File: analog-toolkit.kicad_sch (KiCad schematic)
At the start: 53 parts, among them J1 USB_C, J2 IO, J3 UART, J4 I2C, J5 VBUS, J6 3.3V, J7 OPAMP, J8 ADC, P1 TC2030, Q1 AO3400A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

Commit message: updated kicad files
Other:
- company: (none) -> Jana Hemsing
- title: (none) -> analog-toolkit

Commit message: updated kicad files
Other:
- note added: "20k"
- note added: "3k9"
- note added: "this is fine"

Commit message: updated version
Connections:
- no-connect marks 2 -> 3
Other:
- moved on the sheet: C1, C2, C3, C4, C5, C6, C7, D1, F1, FB1, J1, P1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

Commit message: bumped improved version
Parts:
- C10, C11, C12, C13, C8, C9: value 100n -> 10n
- U3: value STM32G431xB -> STM32G431KBT6
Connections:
- net LED1: now also D1.2 (GK), D1.4 (BA); no longer D1.1 (RK), D1.5 (GA)
- net at Q1.3 (D): now also D1.6 (RA); no longer D1.3 (BK)
- net at R4.2: now also D1.1 (RK); no longer D1.4 (BA)
- net at R2.2: now also D1.3 (BK); no longer D1.6 (RA)
- net at R3.1: now also D1.5 (GA); no longer D1.2 (GK)
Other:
- moved on the sheet: D1
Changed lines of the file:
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@@
 			)
 		)
-		(property "Value" "100n"
+		(property "Value" "10n"
 			(at 210.82 146.05 90)
 			(effects
@@
 			)
 		)
-		(property "Value" "STM32G431xB"
+		(property "Value" "STM32G431KBT6"
 			(at 121.92 105.41 0)
 			(effects
@@
 			)
 		)
-		(property "Value" "100n"
+		(property "Value" "10n"
 			(at 208.28 146.05 90)
 			(effects
@@
 			)
 		)
-		(property "Value" "100n"
+		(property "Value" "10n"
 			(at 213.36 146.05 90)
 			(effects
@@
 			)
 		)
-		(property "Value" "100n"
+		(property "Value" "10n"
 			(at 203.2 146.05 90)
 			(effects
@@
 			)
 		)
-		(property "Value" "100n"
+		(property "Value" "10n"
 			(at 205.74 146.05 90)
 			(effects
@@
 			)
 		)
-		(property "Value" "100n"
+		(property "Value" "10n"
 			(at 200.66 146.05 90)
 			(effects
@@
 	(symbol
 		(lib_id "Device:LED_RGB")
-		(at 143.51 59.69 90)
+		(at 143.51 59.69 270)
 		(unit 1)
 		(exclude_from_sim no)
@@
 		(fields_autoplaced yes)
 		(property "Reference" "D1"
-			(at 152.4 58.4199 90)
+			(at 153.67 58.4199 90)
 			(effects
 				(font
 					(size 1.27 1.27)
 				)
-				(justify right)
+				(justify left)
 			)
 		)
 		(property "Value" "LED_RGB"
-			(at 152.4 60.9599 90)
+			(at 153.67 60.9599 90)
 			(effects
 				(font
 					(size 1.27 1.27)
 				)
-				(justify right)
+				(justify left)
 			)
 		)
 		(property "Footprint" "LED_SMD:LED_RGB_5050-6"
-			(at 144.78 59.69 0)
+			(at 142.24 59.69 0)
 			(effects
 				(font
@@
 		)
 		(property "Datasheet" "~"
-			(at 144.78 59.69 0)
+			(at 142.24 59.69 0)
 			(effects
 				(font

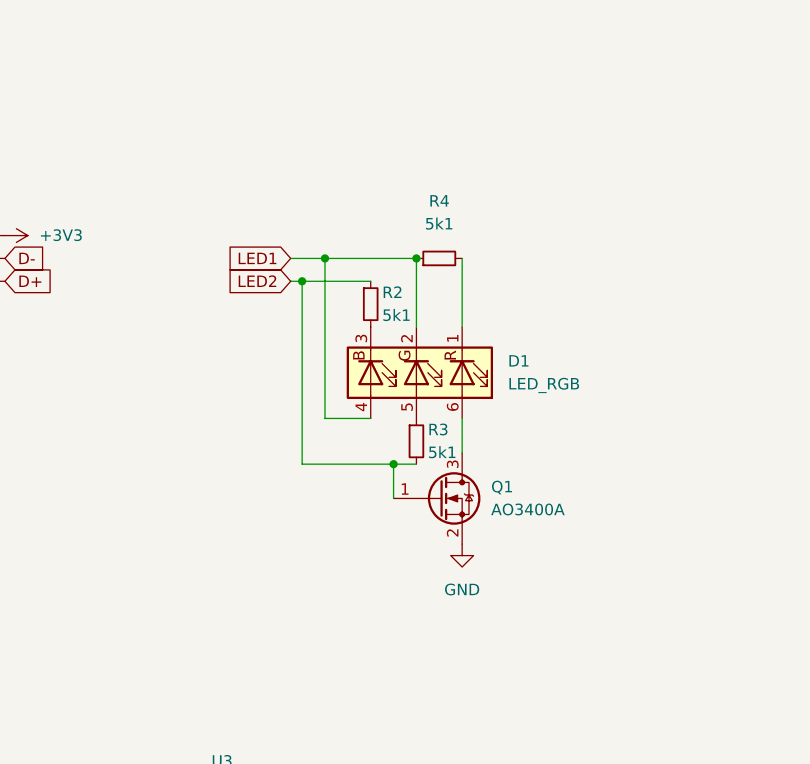
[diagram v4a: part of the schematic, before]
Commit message: updated boards, replaced RGB led
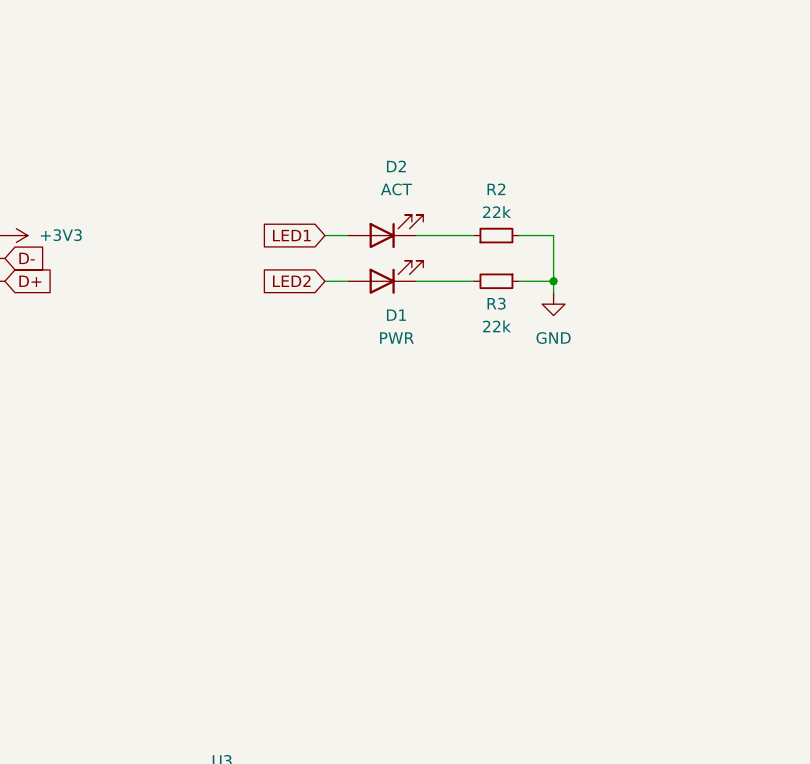
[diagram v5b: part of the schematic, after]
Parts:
- removed D1: LED_RGB, LED_SMD:LED_RGB_5050-6, symbol Device:LED_RGB
- removed Q1: AO3400A, Package_TO_SOT_SMD:SOT-23, symbol Transistor_FET:AO3400A
- removed R4: 5k1, otter:R_0402, symbol Device:R_Small
- added D1: PWR, LED_SMD:LED_0805_2012Metric, symbol Device:LED
- added D2: ACT, LED_SMD:LED_0805_2012Metric, symbol Device:LED
- R2, R3: value 5k1 -> 22k
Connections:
- net GND: now also R2.2, R3.1
- net LED1: now also D2.2 (A)
- net LED2: now also D1.2 (A); no longer R2.1, R3.2
- new net: D2.1 (K), R2.1
- new net: D1.1 (K), R3.2

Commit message: updated board with jlc-specific parts
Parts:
- removed U1: AP2204R-3.3, Package_TO_SOT_SMD:SOT-89-3, symbol Regulator_Linear:AP2204R-3.3
- added U1: AP2204RA-3.3, Package_TO_SOT_SMD:SOT-89-3, symbol Regulator_Linear:AP2204RA-3.3
- C1, C2: JLCPCB (none) -> C19666
- C10, C11, C12, C13, C8, C9: JLCPCB (none) -> C15195
- C3, C4, C5, C6, C7: JLCPCB (none) -> C1525
- D1: JLCPCB (none) -> C34499
- D2: JLCPCB (none) -> C2296
- F1: JLCPCB (none) -> C17477
- FB1: JLCPCB (none) -> C1002
- J1: JLCPCB (none) -> C165948
- R1: JLCPCB (none) -> C25905
- R11, R12, R13, R14, R15, R16: JLCPCB (none) -> C17168
- R2, R3: JLCPCB (none) -> C25768
- SW1: footprint Button_Switch_SMD:SW_SPST_PTS810 -> Button_Switch_SMD:SW_SPST_TS-1088-xR020; JLCPCB (none) -> C720477
- U2: JLCPCB (none) -> C558418
- U3: JLCPCB (none) -> C529357
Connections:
- net +3V3: now also U1.3 (VOUT)
- net GND: now also U1.1 (GND)
- net VBUS: now also U1.2 (VIN)
